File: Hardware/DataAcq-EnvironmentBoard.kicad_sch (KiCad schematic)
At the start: 32 parts, among them J2 CAN Output, J3 CAN Input, J6 Breakout Connector, U1 SHT45, U2 FS3000-1005, U3 LMT87DCK, U4 Daughterboard Connector

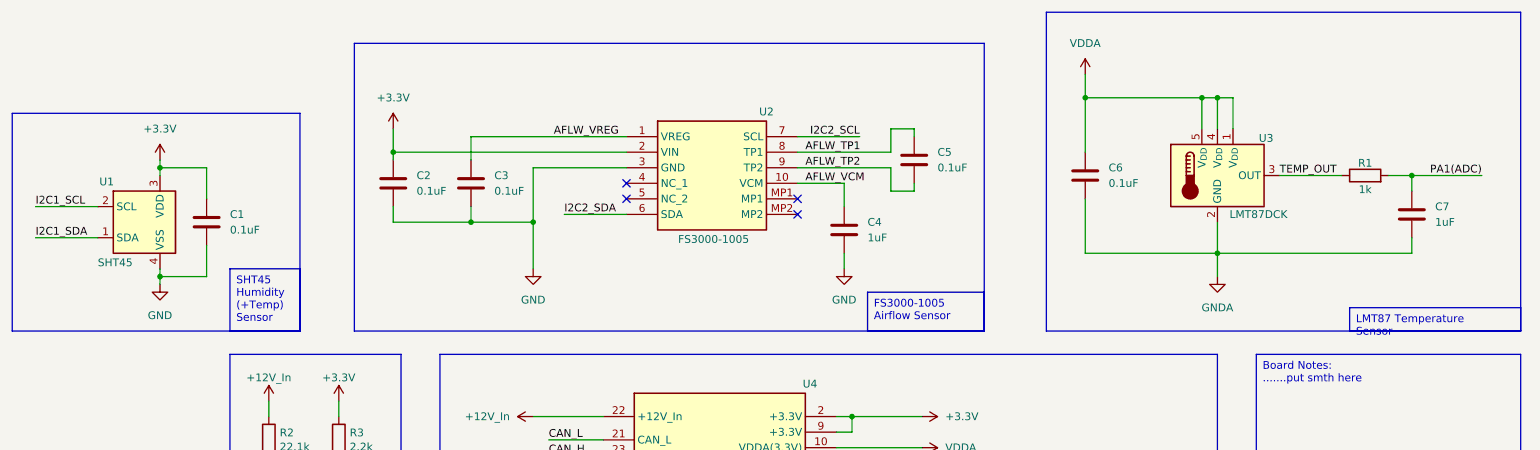
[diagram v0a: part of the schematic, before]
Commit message: remove sensors from this board
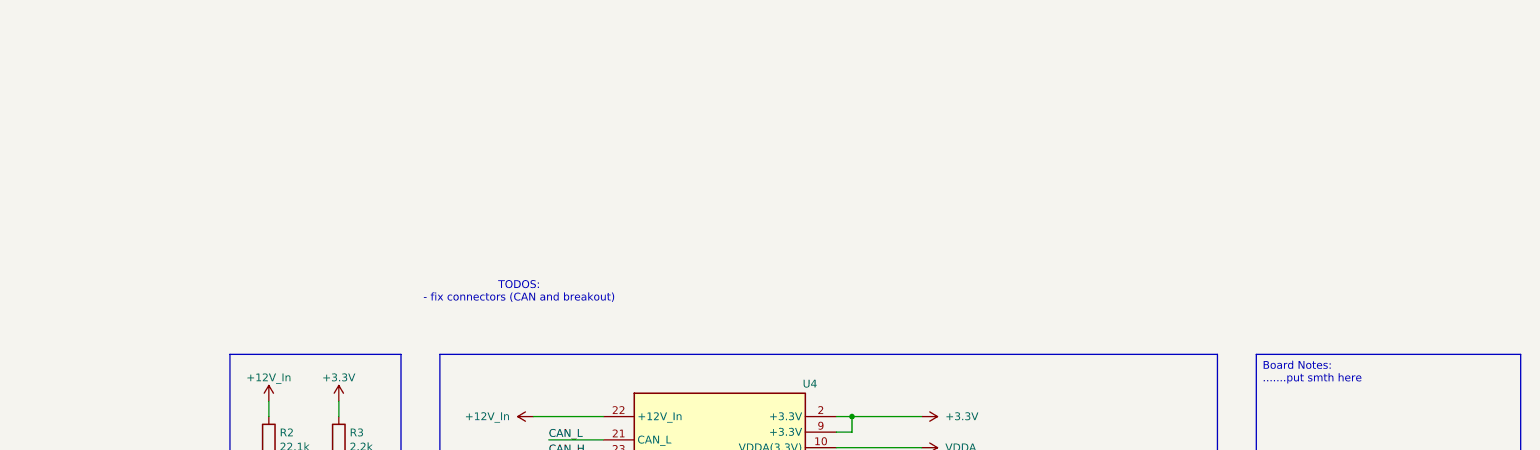
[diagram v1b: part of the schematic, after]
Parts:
- removed C1, C2, C3, C5, C6: 0.1uF, Capacitor_SMD:C_0805_2012Metric, symbol Device:C
- removed C4, C7: 1uF, Capacitor_SMD:C_0805_2012Metric, symbol Device:C
- removed R1: 1k, Resistor_SMD:R_0805_2012Metric, symbol Device:R
- removed U1: SHT45, Sensor_Humidity:Sensirion_DFN-4_1.5x1.5mm_P0.8mm_SHT4x_NoCentralPad, symbol Sensor_Humidity:SHT4x
- removed U2: FS3000-1005, SamacSys_Parts:FS30001005, symbol SamacSys_Parts:FS3000-1005
- removed U3: LMT87DCK, Package_TO_SOT_SMD:SOT-353_SC-70-5, symbol Sensor_Temperature:LMT87DCK
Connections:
- no-connect marks 14 -> 10
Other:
- note added: "TODOS: - fix connectors (CAN and breakout)"

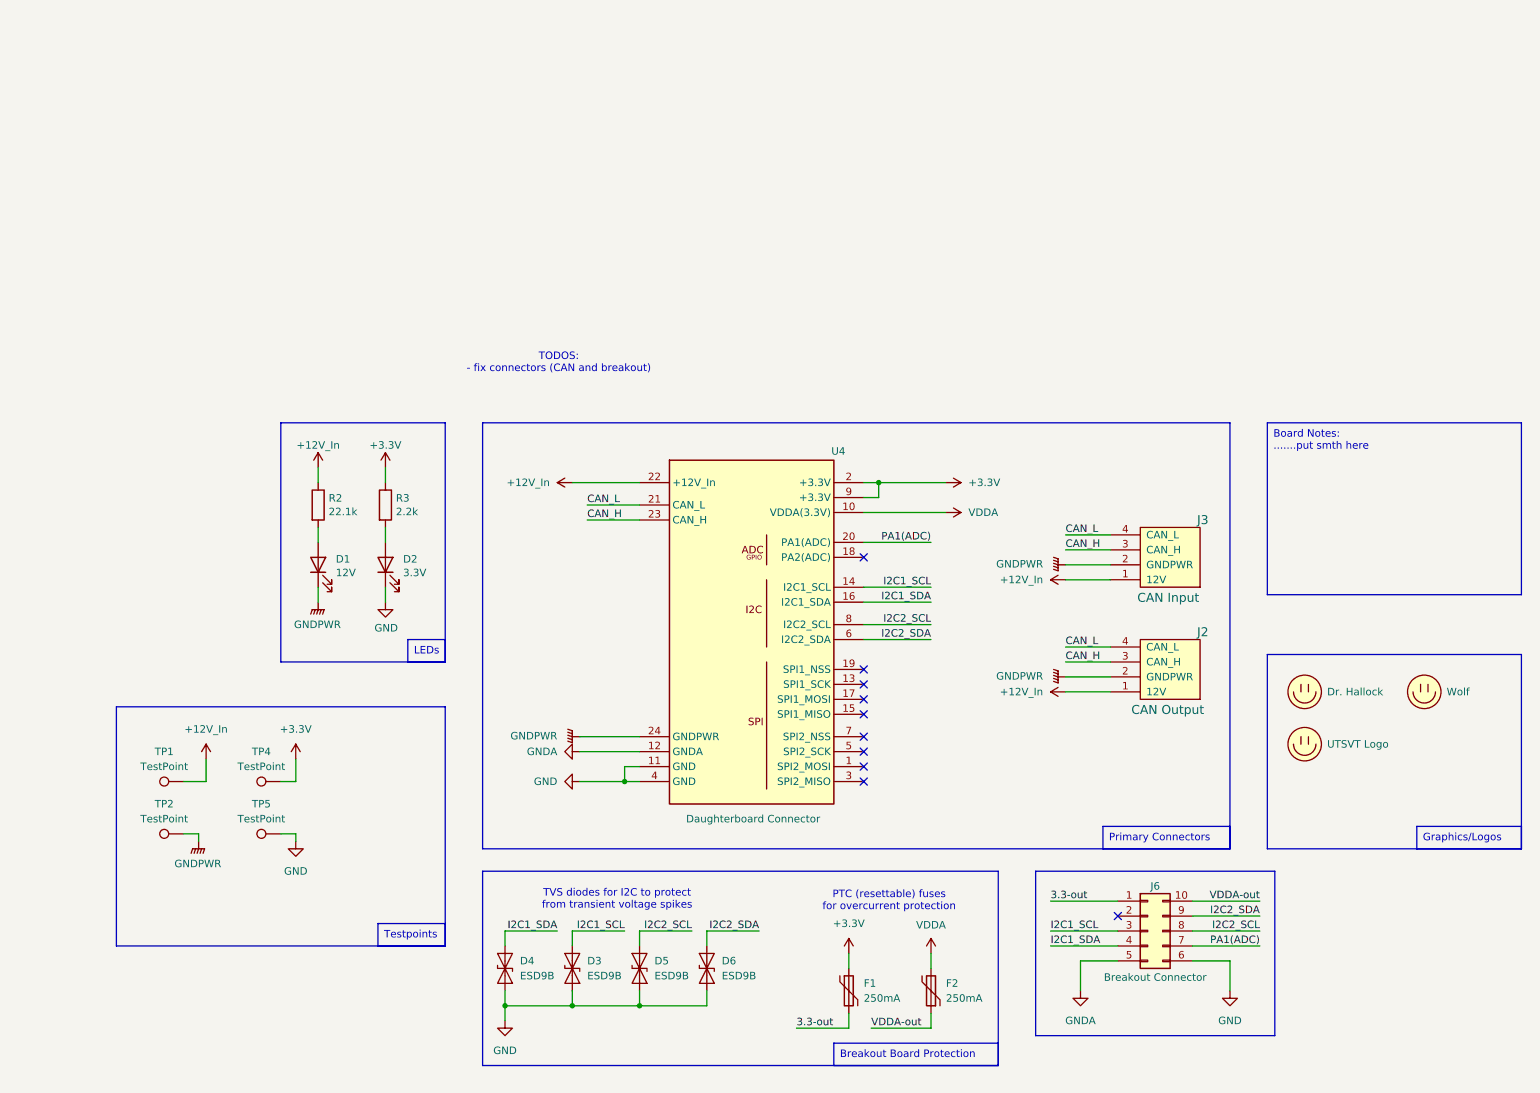
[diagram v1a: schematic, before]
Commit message: rework sch for new breakout design
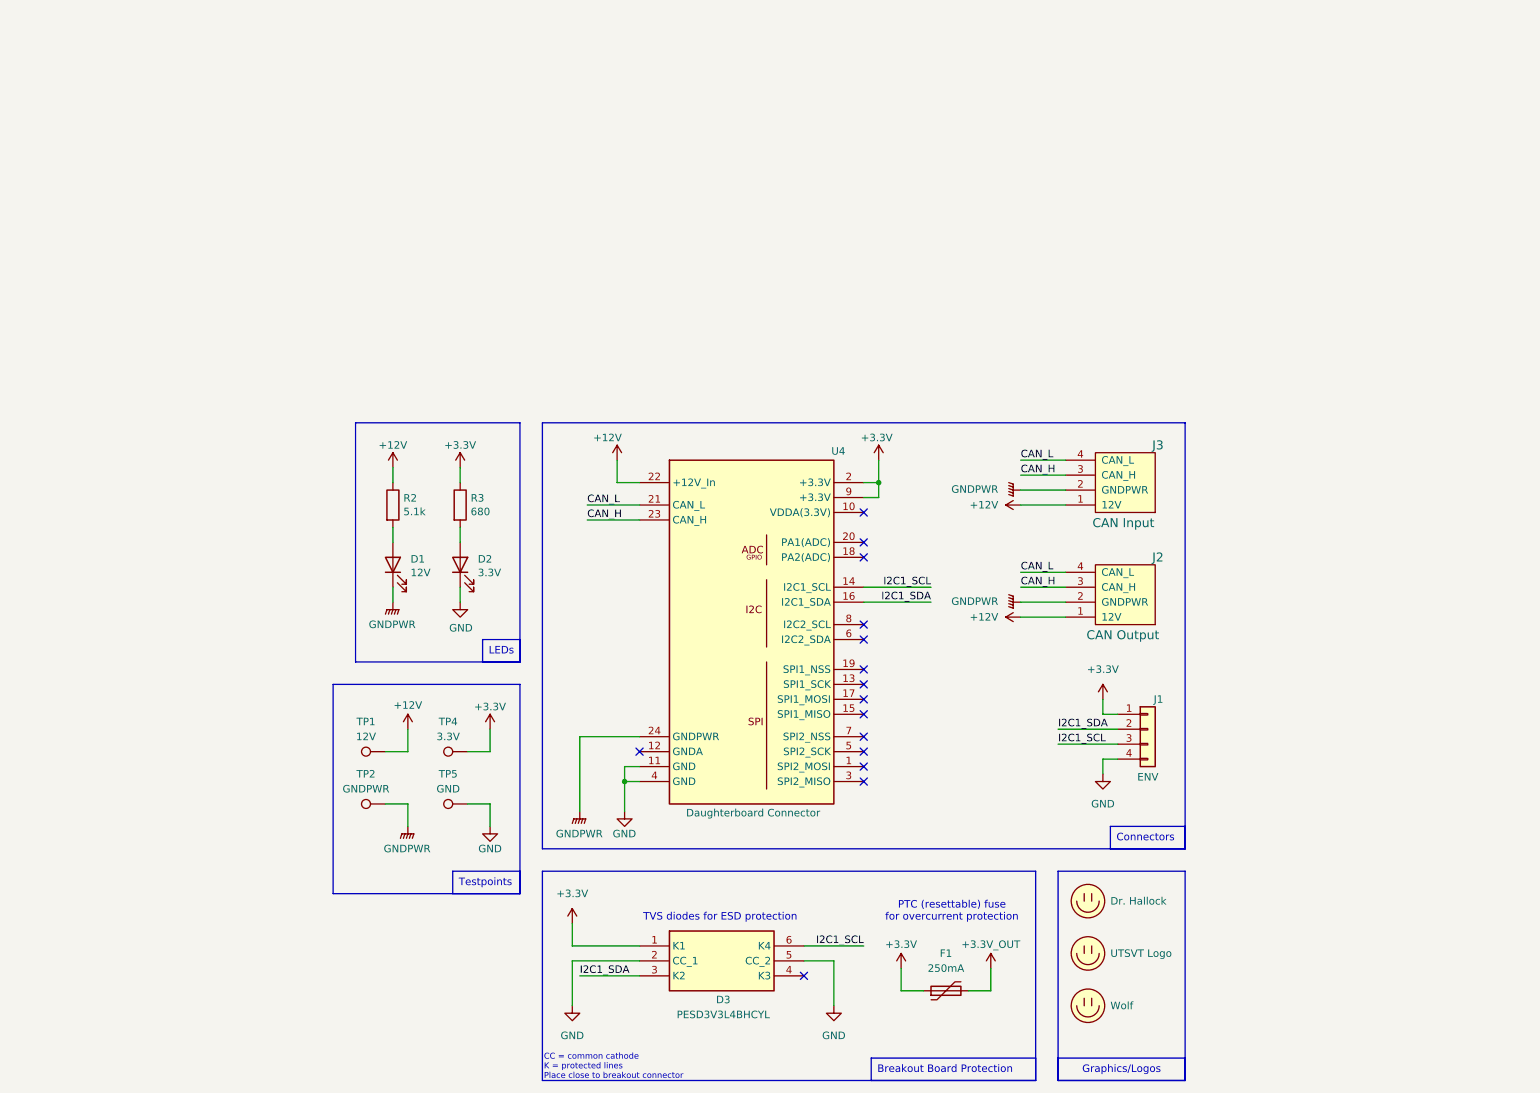
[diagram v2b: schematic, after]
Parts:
- removed D3, D4, D5, D6: ESD9B, Diode_SMD:D_SOD-923, symbol Diode:ESD9B3.3ST5G
- removed F2: 250mA, Fuse:Fuse_0603_1608Metric, symbol Device:Polyfuse
- removed J6: Breakout Connector, Connector_Molex:Molex_Nano-Fit_105310-xx10_2x05_P2.50mm_Vertical, symbol Connector_Generic:Conn_02x05_Counter_Clockwise
- added D3: PESD3V3L4BHCYL, PESD3V3L4BHCYL:SON45P80X130X43-6N, symbol PESD3V3L4BHCYL:PESD3V3L4BHCYL
- added J1: ENV, 1053091104`:MOLEX_1053091104, symbol Connector_Generic:Conn_01x04
- R2: value 22.1k -> 5.1k
- R3: value 2.2k -> 680
- TP1: value TestPoint -> 12V
- TP2: value TestPoint -> GNDPWR
- TP4: value TestPoint -> 3.3V
- TP5: value TestPoint -> GND
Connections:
- net +3.3V: now also D3.1 (K1), J1.1 (Pin_1)
- net GND: now also D3.2 (CC_1), D3.5 (CC_2), J1.4 (Pin_4)
- net I2C1_SCL: now also D3.6 (K4), J1.3 (Pin_3)
- net I2C1_SDA: now also D3.3 (K2), J1.2 (Pin_2)
- net +12V_In renamed +12V
- net 3.3-out renamed +3.3V_OUT
- net GNDA: no longer names the net of U4.12 (GNDA)
- net I2C2_SCL: no longer names the net of U4.8 (I2C2_SCL)
- net I2C2_SDA: no longer names the net of U4.6 (I2C2_SDA)
- net PA1(ADC): no longer names the net of U4.20 (PA1(ADC))
- net VDDA: no longer names the net of U4.10 (VDDA(3.3V))
- no-connect marks 10 -> 15
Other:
- note added: "CC = common cathode K = protected lines Place close to breakout connector"
- note added: "PTC (resettable) fuse for overcurrent protection"
- note added: "TVS diodes for ESD protection"
- note removed: "PTC (resettable) fuses for overcurrent protection"
- note removed: "TODOS: - fix connectors (CAN and breakout)"
- note removed: "TVS diodes for I2C to protect from transient voltage spikes"
- moved on the sheet: D1, D2, F1, J2, J3, R2, R3, TP1, TP2, TP4, TP5

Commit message: new ptc & footprints
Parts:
- F1: footprint Fuse:Fuse_0603_1608Metric -> Fuse:Fuse_1206_3216Metric; P/N 0ZCM0010FF2G -> 1206L010/60WR
- J1: footprint 1053091104`:MOLEX_1053091104 -> 1053091104:MOLEX_1053091104
- R2: P/N CRCW080522K1FKEA -> (none)
- R3: P/N SDR10EZPF2200 -> (none)
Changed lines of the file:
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@@
 			)
 		)
-		(property "Footprint" "1053091104`:MOLEX_1053091104"
+		(property "Footprint" "1053091104:MOLEX_1053091104"
 			(at 208.28 137.16 0)
 			(effects
@@
 			)
 		)
-		(property "Footprint" "Fuse:Fuse_0603_1608Metric"
+		(property "Footprint" "Fuse:Fuse_1206_3216Metric"
 			(at 179.07 180.34 0)
 			(effects
@@
 			)
 		)
-		(property "Datasheet" "https://www.mouser.com/ProductDetail/530-0ZCM0010FF2G"
+		(property "Datasheet" "https://www.littelfuse.com/assetdocs/resettable-ptcs-1206l-datasheet?assetguid=2b6a1515-d4ee-4c83-8bd4-152b4901b8f5"
 			(at 173.99 181.61 0)
 			(effects
@@
 			)
 		)
-		(property "P/N" "0ZCM0010FF2G"
+		(property "P/N" "1206L010/60WR "
 			(at 173.99 181.61 0)
 			(effects
@@
 			)
 		)
-		(property "P/N" "CRCW080522K1FKEA"
+		(property "P/N" ""
 			(at 80.01 99.06 0)
 			(effects
@@
 			)
 		)
-		(property "P/N" "SDR10EZPF2200"
+		(property "P/N" ""
 			(at 91.44 99.06 0)
 			(effects

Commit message: dumb and dumber
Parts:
- J2: value CAN Output -> CAN OUT
- J3: value CAN Input -> CAN IN
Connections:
- net +3.3V: no longer D3.1 (K1), J1.1 (Pin_1)
- net +3.3V_OUT: now also D3.1 (K1), J1.1 (Pin_1)
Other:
- company: (none) -> LHRs
- moved on the sheet: D1, D2, D3, F1, J1, J2, J3, R2, R3, TP1, TP2, TP4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
